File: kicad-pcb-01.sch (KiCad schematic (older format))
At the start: 5 parts

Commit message: mcu ready part 3
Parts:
- added C? (x4): 0.1uF, symbol Device:C_Small
- added C? (x2): 22pF, symbol Device:C_Small
- added R?: 10k, symbol Device:R_Small
- added SW?: SW_Push, symbol Switch:SW_Push
- added Y?: 16MHz, symbol Device:Crystal_GND24_Small
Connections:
- net labels added: D+, D-
- wire segments 15 -> 45
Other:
- moved on the sheet: C?, R?, U?

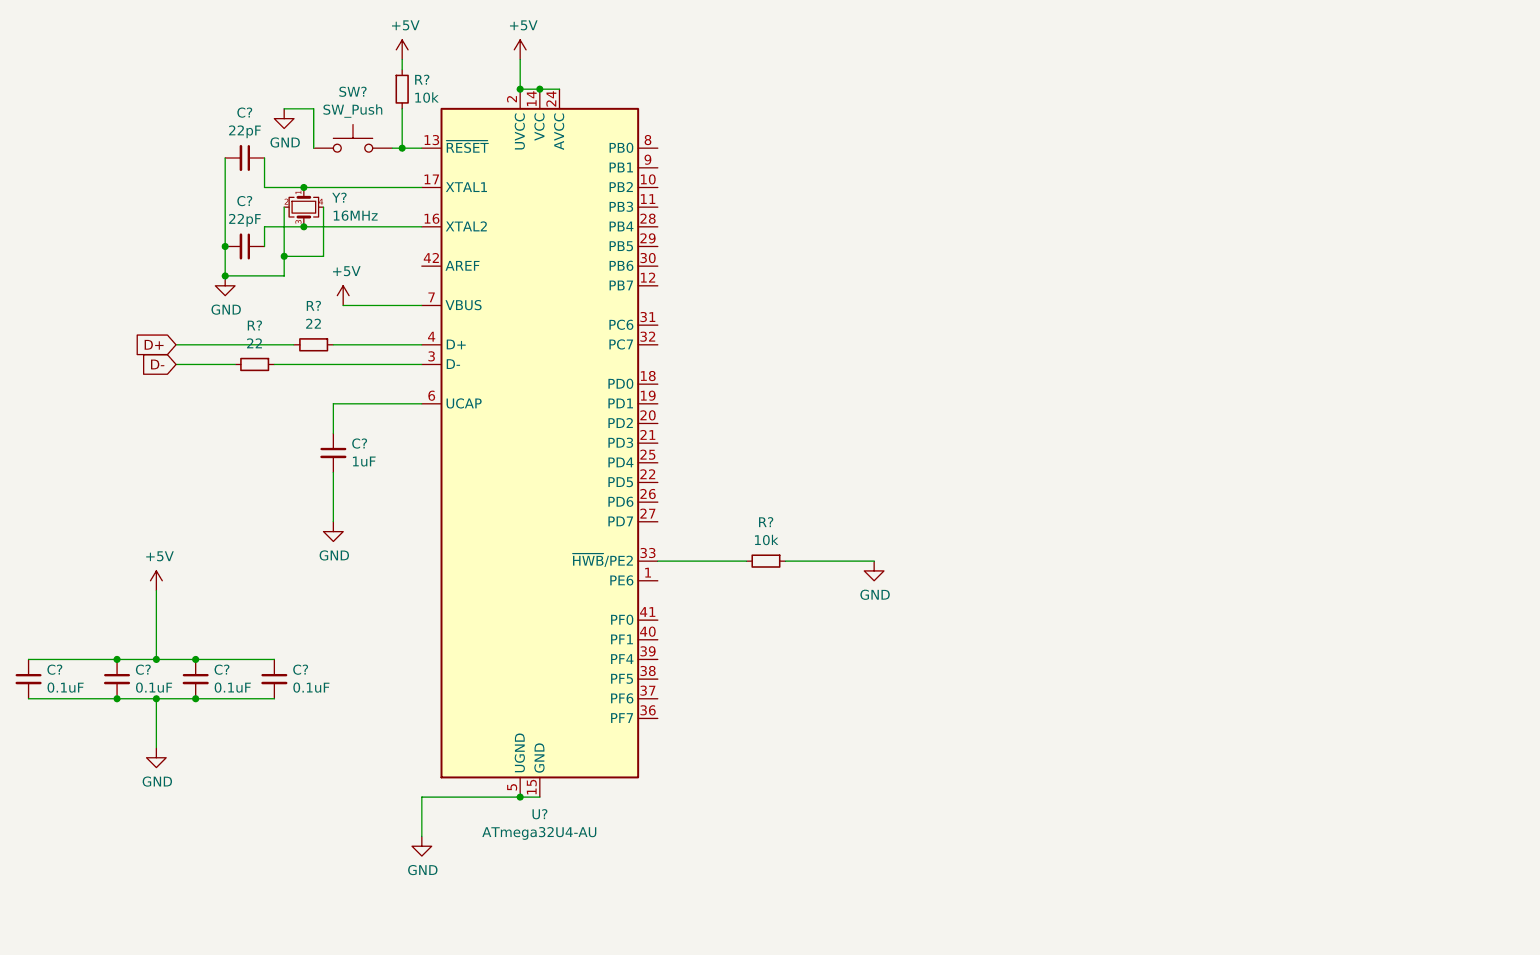
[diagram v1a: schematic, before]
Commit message: added usb and switches, labeled all pcb parts and mapped them to components
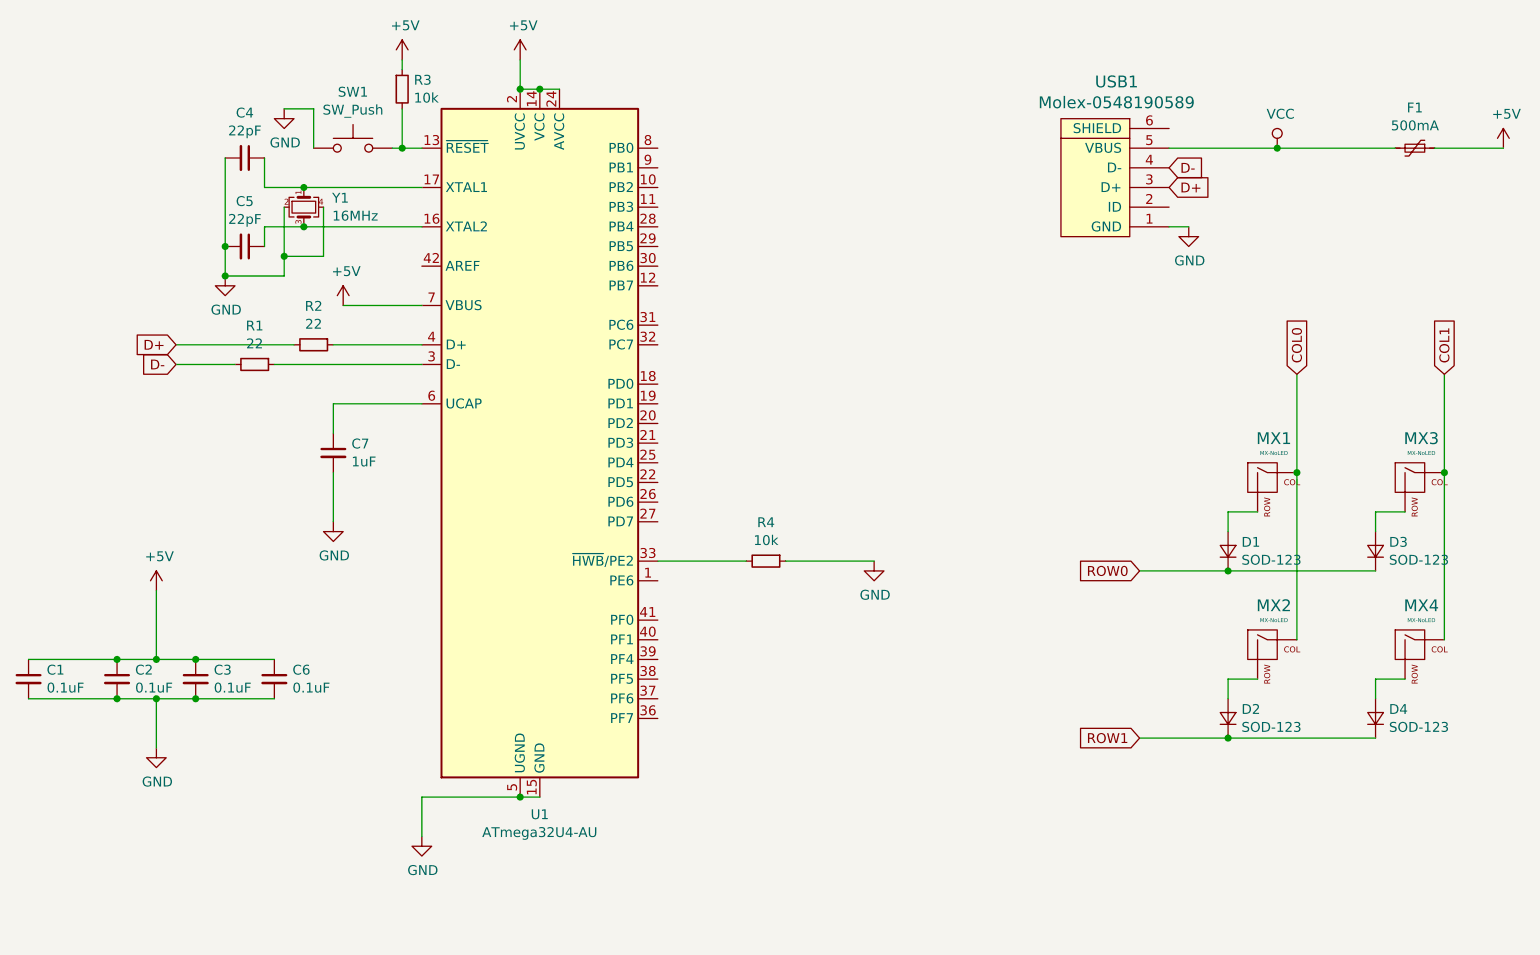
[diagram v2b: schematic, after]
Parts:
- added D1, D2, D3, D4: SOD-123, Diode_SMD:D_SOD-123, symbol Device:D_Small
- added F1: 500mA, Fuse:Fuse_1206_3216Metric, symbol Device:Polyfuse_Small
- added MX1, MX2, MX3, MX4: MX-NoLED, MX_Alps_Hybrid:MX-1U-NoLED, symbol MX_Alps_Hybrid:MX-NoLED
- added USB1: Molex-0548190589, random-keyboard-parts:Molex-0548190589, symbol random-keyboard-parts:Molex-0548190589
- C1, C2, C3, C4, C5, C6, C7: renamed from C?; footprint (none) -> Capacitor_SMD:C_0805_2012Metric
- R1, R2, R3, R4: renamed from R?; footprint (none) -> Resistor_SMD:R_0805_2012Metric
- SW1: renamed from SW?; footprint (none) -> random-keyboard-parts:SKQG-1155865
- Y1: renamed from Y?; footprint (none) -> Crystal:Crystal_SMD_3225-4Pin_3.2x2.5mm
- gave numbers to parts that had none: 1
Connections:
- net +5V: now also F1.1
- net D+: now also USB1.3 (D+)
- net D-: now also USB1.4 (D-)
- net GND: now also USB1.1 (GND)
- new net: D1.2 (A), MX1.2 (ROW)
- new net: D3.2 (A), MX3.2 (ROW)
- new net: D4.2 (A), MX4.2 (ROW)
- new net: D2.2 (A), MX2.2 (ROW)
- new net COL0: MX1.1 (COL), MX2.1 (COL)
- new net COL1: MX3.1 (COL), MX4.1 (COL)
- new net ROW0: D1.1 (K), D3.1 (K)
- new net ROW1: D2.1 (K), D4.1 (K)
- new net VCC: F1.2, USB1.5 (VBUS)

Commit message: pcb layout
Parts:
- C6: value 0.1uF -> 10uF
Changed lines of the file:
@@
 P 2100 4050
 F 0 "C6" H 2192 4096 50  0000 L CNN
-F 1 "0.1uF" H 2192 4005 50  0000 L CNN
+F 1 "10uF" H 2192 4005 50  0000 L CNN
 F 2 "Capacitor_SMD:C_0805_2012Metric" H 2100 4050 50  0001 C CNN
 F 3 "~" H 2100 4050 50  0001 C CNN

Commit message: routing complete
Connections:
- net COL0: now also U1.29 (PB5)
- net COL1: now also U1.28 (PB4)
- net ROW0: now also U1.27 (PD7)
- net ROW1: now also U1.26 (PD6)
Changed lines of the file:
@@
 Text GLabel 8050 2500 1    50   Input ~ 0
 COL1
+Text GLabel 4050 3150 2    50   Input ~ 0
+ROW1
+Text GLabel 4050 3250 2    50   Input ~ 0
+ROW0
+Text GLabel 4050 1750 2    50   Input ~ 0
+COL1
+Text GLabel 4050 1850 2    50   Input ~ 0
+COL0
 $EndSCHEMATC

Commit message: added lcsc part ref:
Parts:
- C1, C2, C3: LCSC (none) -> C1711
- C4, C5: LCSC (none) -> C465168
- C6: LCSC (none) -> C307520
- C7: LCSC (none) -> C116352
- D1, D2, D3, D4: LCSC (none) -> C77978
- F1: LCSC (none) -> C151162
- R1, R2: LCSC (none) -> C413152
- R3, R4: LCSC (none) -> C191101
- SW1: LCSC (none) -> C221929
- U1: LCSC (none) -> C44854
- USB1: LCSC (none) -> C105424
- Y1: LCSC (none) -> C254367
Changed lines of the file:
@@
 F 2 "Package_QFP:TQFP-44_10x10mm_P0.8mm" H 3450 2850 50  0001 C CIN
 F 3 "http://ww1.microchip.com/downloads/en/DeviceDoc/Atmel-7766-8-bit-AVR-ATmega16U4-32U4_Datasheet.pdf" H 3450 2850 50  0001 C CNN
+F 4 "C44854" H 3450 2850 50  0001 C CNN "LCSC"
 	1    3450 2850
 	1    0    0    -1
@@
 F 2 "Resistor_SMD:R_0805_2012Metric" H 4600 3450 50  0001 C CNN
 F 3 "~" H 4600 3450 50  0001 C CNN
+F 4 "C191101" V 4600 3450 50  0001 C CNN "LCSC"
 	1    4600 3450
 	0    1    1    0
@@
 F 2 "Resistor_SMD:R_0805_2012Metric" H 2300 2350 50  0001 C CNN
 F 3 "~" H 2300 2350 50  0001 C CNN
+F 4 "C413152" V 2300 2350 50  0001 C CNN "LCSC"
 	1    2300 2350
 	0    1    1    0
@@
 F 2 "Resistor_SMD:R_0805_2012Metric" H 2000 2450 50  0001 C CNN
 F 3 "~" H 2000 2450 50  0001 C CNN
+F 4 "C413152" V 2000 2450 50  0001 C CNN "LCSC"
 	1    2000 2450
 	0    1    1    0
@@
 F 2 "Capacitor_SMD:C_0805_2012Metric" H 2400 2900 50  0001 C CNN
 F 3 "~" H 2400 2900 50  0001 C CNN
+F 4 "C116352" H 2400 2900 50  0001 C CNN "LCSC"
 	1    2400 2900
 	1    0    0    -1
@@
 F 2 "Capacitor_SMD:C_0805_2012Metric" H 850 4050 50  0001 C CNN
 F 3 "~" H 850 4050 50  0001 C CNN
+F 4 "C1711" H 850 4050 50  0001 C CNN "LCSC"
 	1    850  4050
 	1    0    0    -1
@@
 F 2 "Capacitor_SMD:C_0805_2012Metric" H 1300 4050 50  0001 C CNN
 F 3 "~" H 1300 4050 50  0001 C CNN
+F 4 "C1711" H 1300 4050 50  0001 C CNN "LCSC"
 	1    1300 4050
 	1    0    0    -1
@@
 F 2 "Capacitor_SMD:C_0805_2012Metric" H 1700 4050 50  0001 C CNN
 F 3 "~" H 1700 4050 50  0001 C CNN
+F 4 "C1711" H 1700 4050 50  0001 C CNN "LCSC"
 	1    1700 4050
 	1    0    0    -1
@@
 F 2 "Capacitor_SMD:C_0805_2012Metric" H 2100 4050 50  0001 C CNN
 F 3 "~" H 2100 4050 50  0001 C CNN
+F 4 "C307520" H 2100 4050 50  0001 C CNN "LCSC"
 	1    2100 4050
 	1    0    0    -1
@@
 F 2 "Crystal:Crystal_SMD_3225-4Pin_3.2x2.5mm" H 2250 1650 50  0001 C CNN
 F 3 "~" H 2250 1650 50  0001 C CNN
+F 4 "C254367" V 2250 1650 50  0001 C CNN "LCSC"
 	1    2250 1650
 	0    1    1    0
@@
 F 2 "Capacitor_SMD:C_0805_2012Metric" H 1950 1400 50  0001 C CNN
 F 3 "~" H 1950 1400 50  0001 C CNN
+F 4 "C465168" V 1950 1400 50  0001 C CNN "LCSC"
 	1    1950 1400
 	0    1    1    0
@@
 F 2 "Capacitor_SMD:C_0805_2012Metric" H 1950 1850 50  0001 C CNN
 F 3 "~" H 1950 1850 50  0001 C CNN
+F 4 "C465168" V 1950 1850 50  0001 C CNN "LCSC"
 	1    1950 1850
 	0    1    1    0
@@
 F 2 "random-keyboard-parts:SKQG-1155865" H 2500 1550 50  0001 C CNN
 F 3 "~" H 2500 1550 50  0001 C CNN
+F 4 "C221929" H 2500 1350 50  0001 C CNN "LCSC"
 	1    2500 1350
 	1    0    0    -1
@@
 F 2 "Resistor_SMD:R_0805_2012Metric" H 2750 1050 50  0001 C CNN
 F 3 "~" H 2750 1050 50  0001 C CNN
+F 4 "C191101" H 2750 1050 50  0001 C CNN "LCSC"
 	1    2750 1050
 	1    0    0    -1
@@
 F 2 "random-keyboard-parts:Molex-0548190589" H 6350 1550 60  0001 C CNN
 F 3 "" H 6350 1550 60  0001 C CNN
+F 4 "C105424" V 6350 1550 50  0001 C CNN "LCSC"
 	1    6350 1550
 	0    -1   -1   0
@@
 F 2 "Fuse:Fuse_1206_3216Metric" H 7950 1150 50  0001 L CNN
 F 3 "~" H 7900 1350 50  0001 C CNN
+F 4 "C151162" V 7900 1350 50  0001 C CNN "LCSC"
 	1    7900 1350
 	0    1    1    0
@@
 F 2 "Diode_SMD:D_SOD-123" V 6950 3400 50  0001 C CNN
 F 3 "~" V 6950 3400 50  0001 C CNN
+F 4 "C77978" V 6950 3400 50  0001 C CNN "LCSC"
 	1    6950 3400
 	0    -1   -1   0
@@
 F 2 "Diode_SMD:D_SOD-123" V 7700 3400 50  0001 C CNN
 F 3 "~" V 7700 3400 50  0001 C CNN
+F 4 "C77978" V 7700 3400 50  0001 C CNN "LCSC"
 	1    7700 3400
 	0    -1   -1   0
@@
 F 2 "Diode_SMD:D_SOD-123" V 7700 4250 50  0001 C CNN
 F 3 "~" V 7700 4250 50  0001 C CNN
+F 4 "C77978" V 7700 4250 50  0001 C CNN "LCSC"
 	1    7700 4250
 	0    -1   -1   0
@@
 F 2 "Diode_SMD:D_SOD-123" V 6950 4250 50  0001 C CNN
 F 3 "~" V 6950 4250 50  0001 C CNN
+F 4 "C77978" V 6950 4250 50  0001 C CNN "LCSC"
 	1    6950 4250
 	0    -1   -1   0
